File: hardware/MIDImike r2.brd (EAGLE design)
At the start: 84.8 x 53.3 mm, 8 parts, among them SW1 PUSH-BTN, SW2 SH-7030TB

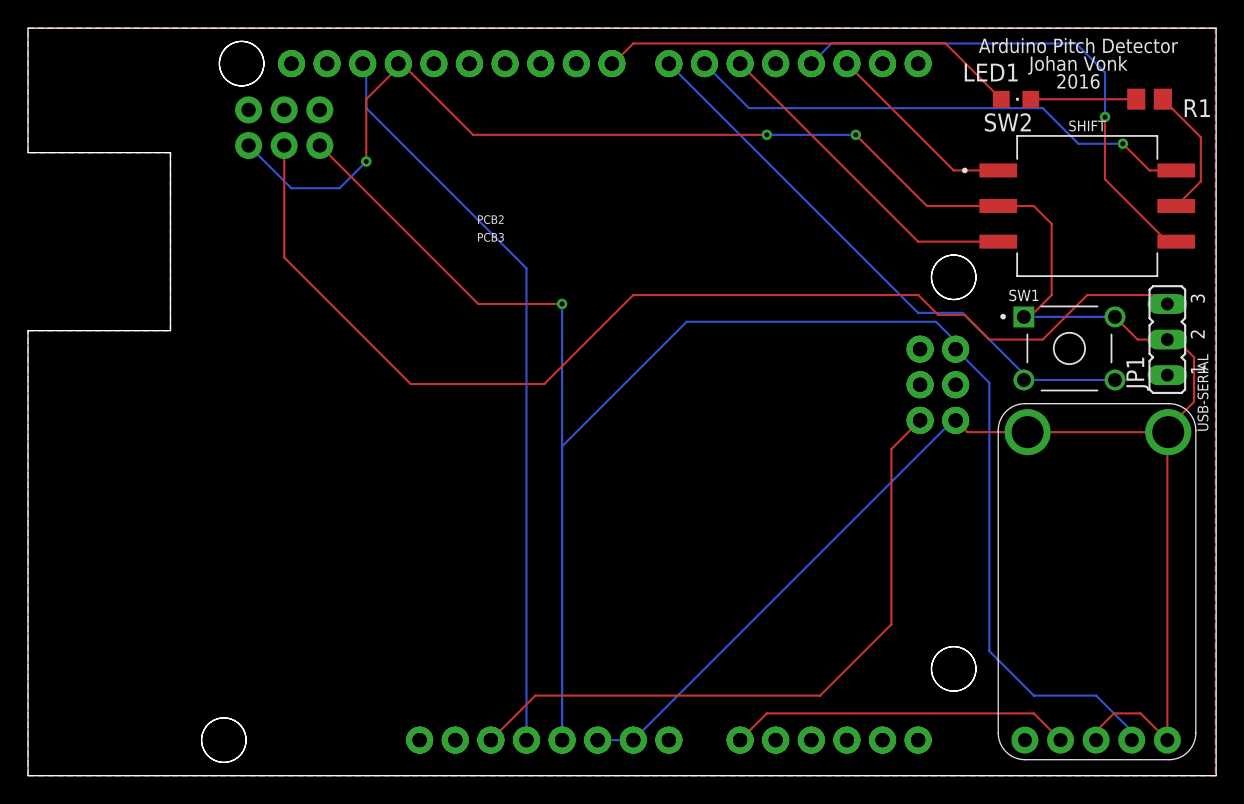
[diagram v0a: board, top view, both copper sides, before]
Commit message: fix so that USB-MIDI connects to MISO2
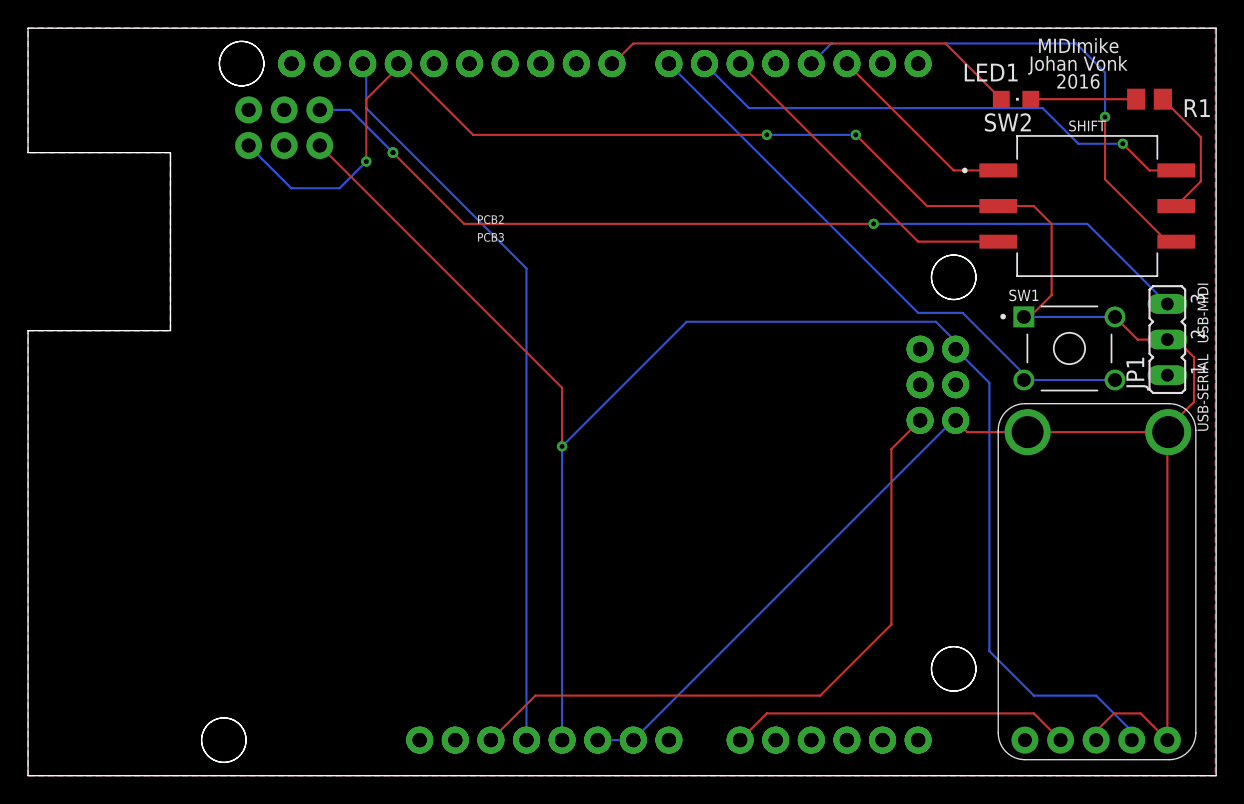
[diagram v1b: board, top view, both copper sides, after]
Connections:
- net N$3: now also PCB2.MISO2; no longer PCB2.MOSI2
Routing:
- net 5V: track 142.6 -> 118.2 mm
- net N$3: track 80.3 -> 66.2 mm, vias 0 -> 3
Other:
- board text added: "MIDImike"
- board text added: "https://github.com/jvonk/MIDImike"
- board text removed: "Arduino Pitch Detector"
- board text removed: "https://github.com/jvonk/Arduino_Pitch-Detector"
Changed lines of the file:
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@@
 <wire x1="10.16" y1="31.75" x2="0" y2="31.75" width="0" layer="20"/>
 <wire x1="0" y1="31.75" x2="0" y2="0" width="0" layer="20"/>
-<text x="83.82" y="33.02" size="0.762" layer="22" rot="R90" align="center">USB-MIDI</text>
+<text x="83.82" y="33.02" size="0.762" layer="21" rot="R90" align="center">USB-MIDI</text>
 <text x="83.82" y="27.305" size="0.762" layer="21" rot="R90" align="center">USB-SERIAL</text>
-<text x="74.93" y="52.07" size="1.016" layer="21" align="center">Arduino Pitch Detector</text>
+<text x="74.93" y="52.07" size="1.016" layer="21" align="center">MIDImike</text>
 <text x="74.93" y="50.8" size="1.016" layer="21" align="center">Johan Vonk</text>
 <text x="74.93" y="49.53" size="1.016" layer="21" align="center">2016</text>
-<text x="53.34" y="25.4" size="1.27" layer="22" rot="MR0">https://github.com/jvonk/Arduino_Pitch-Detector</text>
+<text x="53.34" y="25.4" size="2.032" layer="22" rot="MR0">https://github.com/jvonk/MIDImike</text>
 <text x="75.565" y="46.355" size="0.762" layer="21" rot="R180" align="center">SHIFT</text>
 </plain>
@@
 <wire x1="38.1" y1="23.495" x2="46.99" y2="32.385" width="0.1524" layer="16"/>
 <wire x1="46.99" y1="32.385" x2="64.77" y2="32.385" width="0.1524" layer="16"/>
-<wire x1="20.81560625" y1="44.9587875" x2="32.11939375" y2="33.655" width="0.1524" layer="1"/>
-<wire x1="32.11939375" y1="33.655" x2="38.1" y2="33.655" width="0.1524" layer="1"/>
-<via x="38.1" y="33.655" extent="1-16" drill="0.35"/>
-<wire x1="38.1" y1="33.655" x2="38.1" y2="2.54" width="0.1524" layer="16"/>
+<via x="38.1" y="23.495" extent="1-16" drill="0.35"/>
+<wire x1="38.1" y1="27.67439375" x2="38.1" y2="23.495" width="0.1524" layer="1"/>
+<wire x1="20.81560625" y1="44.9587875" x2="38.1" y2="27.67439375" width="0.1524" layer="1"/>
 </signal>
 <signal name="A0">
@@
 <contactref element="PCB2" pad="D4"/>
 </signal>
-<signal name="N$3">
-<contactref element="PCB2" pad="MOSI2"/>
-<contactref element="JP1" pad="3"/>
-<wire x1="68.58" y1="31.115" x2="66.8147" y2="32.8803" width="0.1524" layer="1"/>
-<wire x1="72.39" y1="31.115" x2="75.565" y2="34.29" width="0.1524" layer="1"/>
-<wire x1="75.565" y1="34.29" x2="80.645" y2="34.29" width="0.1524" layer="1"/>
-<wire x1="80.645" y1="34.29" x2="81.28" y2="33.655" width="0.1524" layer="1"/>
-<wire x1="68.58" y1="31.115" x2="72.39" y2="31.115" width="0.1524" layer="1"/>
-<wire x1="66.8147" y1="32.8803" x2="64.93003125" y2="32.8803" width="0.1524" layer="1"/>
-<wire x1="64.93003125" y1="32.8803" x2="63.52033125" y2="34.29" width="0.1524" layer="1"/>
-<wire x1="43.18" y1="34.29" x2="36.83" y2="27.94" width="0.1524" layer="1"/>
-<wire x1="36.83" y1="27.94" x2="27.305" y2="27.94" width="0.1524" layer="1"/>
-<wire x1="18.27560625" y1="36.96939375" x2="18.27560625" y2="44.9587875" width="0.1524" layer="1"/>
-<wire x1="63.52033125" y1="34.29" x2="43.18" y2="34.29" width="0.1524" layer="1"/>
-<wire x1="27.305" y1="27.94" x2="18.27560625" y2="36.96939375" width="0.1524" layer="1"/>
-</signal>
 <signal name="N$8">
 <contactref element="LED1" pad="C"/>
@@
 <wire x1="76.835" y1="46.99" x2="76.835" y2="50.165" width="0.1524" layer="16"/>
 </signal>
+<signal name="N$3">
+<contactref element="JP1" pad="3"/>
+<contactref element="PCB2" pad="MISO2"/>
+<wire x1="81.28" y1="33.655" x2="75.565" y2="39.37" width="0.1524" layer="16"/>
+<wire x1="75.565" y1="39.37" x2="60.325" y2="39.37" width="0.1524" layer="16"/>
+<via x="60.325" y="39.37" extent="1-16" drill="0.35"/>
+<wire x1="60.325" y1="39.37" x2="31.115" y2="39.37" width="0.1524" layer="1"/>
+<wire x1="31.115" y1="39.37" x2="26.035" y2="44.45" width="0.1524" layer="1"/>
+<via x="26.035" y="44.45" extent="1-16" drill="0.35"/>
+<via x="26.035" y="44.45" extent="1-16" drill="0.35"/>
+<wire x1="20.81560625" y1="47.4987875" x2="22.9862125" y2="47.4987875" width="0.1524" layer="16"/>
+<wire x1="22.9862125" y1="47.4987875" x2="26.035" y2="44.45" width="0.1524" layer="16"/>
+</signal>
 </signals>
